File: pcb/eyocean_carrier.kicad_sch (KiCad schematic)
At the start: 9 parts, among them J1 SuperMini_L (TX..GPIO7), J2 SuperMini_R (5V..GPIO8), J3 CC1101_433MHz

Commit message: pcb: use 0603 for both decoupling capacitors
Move the 10 uF CC1101 decoupling cap from 0805 to the same 0603
hand-solder footprint as the 100 nF (use X5R, >= 6.3 V). Regenerated
schematic and board (3V3 rail and pad-1 positions unchanged), ERC/DRC
with schematic parity clean, JLCPCB Gerbers re-exported.
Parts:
- C2: footprint Capacitor_SMD:C_0805_2012Metric_Pad1.18x1.45mm_HandSolder -> Capacitor_SMD:C_0603_1608Metric_Pad1.08x0.95mm_HandSolder
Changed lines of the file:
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@@
 			)
 		)
-		(property "Footprint" "Capacitor_SMD:C_0805_2012Metric_Pad1.18x1.45mm_HandSolder"
+		(property "Footprint" "Capacitor_SMD:C_0603_1608Metric_Pad1.08x0.95mm_HandSolder"
 			(at 154.94 114.3 0)
 			(hide yes)

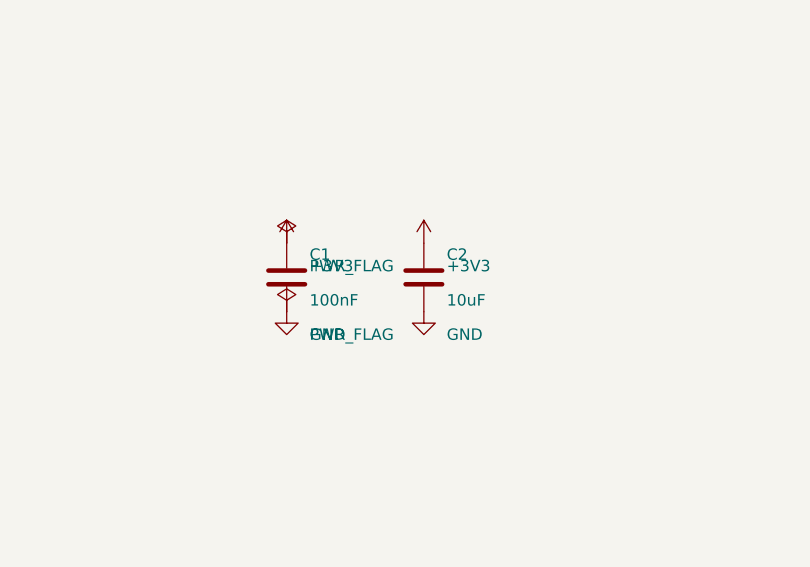
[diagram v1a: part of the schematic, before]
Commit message: pcb: single 10 uF decoupling capacitor
The CC1101 module already carries its own 100 nF next to the chip, so
the carrier only needs a local bulk cap for the TX current bursts. Drop
C2 and make C1 a 10 uF 0603 X5R 10 V (LCSC C19702, Samsung
CL10A106KP8NNNC); its GND stitching via now sits beside its pad.
Regenerated schematic and board, ERC/DRC with schematic parity clean,
JLCPCB Gerbers re-exported.
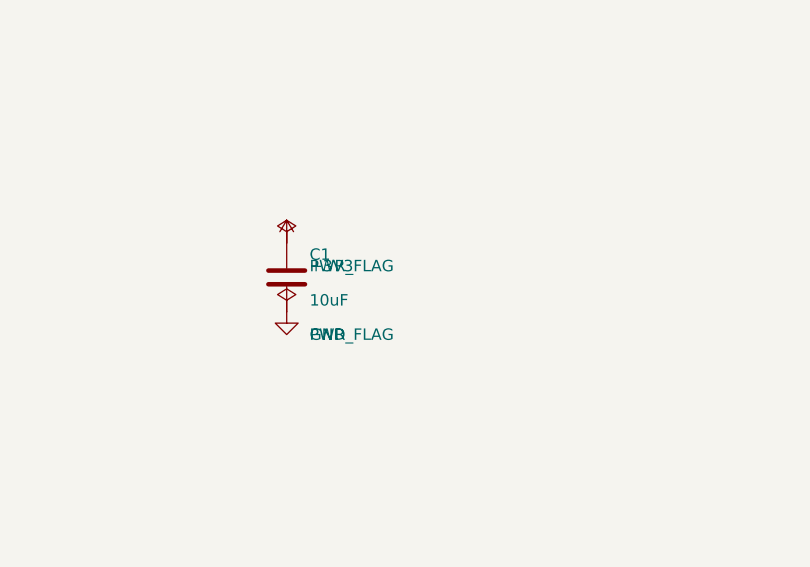
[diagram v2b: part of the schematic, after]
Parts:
- removed C2: 10uF, Capacitor_SMD:C_0603_1608Metric_Pad1.08x0.95mm_HandSolder, symbol Device:C
- C1: value 100nF -> 10uF
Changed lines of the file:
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@@
 			)
 		)
-		(property "Value" "100nF"
+		(property "Value" "10uF"
 			(at 142.24 116.84 0)
 			(show_name no)
@@
 			)
 		)
-		(property "Description" "CC1101 VDD decoupling"
+		(property "Description" "CC1101 VDD bulk decoupling, 10 uF X5R >= 10 V"
 			(at 139.7 114.3 0)
 			(hide yes)
@@
 					(unit 1)
 				)
-			)
-		)
-	)
-	(symbol
-		(lib_id "Device:C")
-		(at 154.94 114.3 0)
-		(unit 1)
-		(body_style 1)
-		(exclude_from_sim no)
-		(in_bom yes)
-		(on_board yes)
-		(in_pos_files yes)
-		(dnp no)
-		(property "Reference" "C2"
-			(at 157.48 111.76 0)
-			(show_name no)
-			(do_not_autoplace no)
-			(effects
-				(font
-					(size 1.27 1.27)
-				)
-				(justify left)
-			)
-		)
-		(property "Value" "10uF"
-			(at 157.48 116.84 0)
-			(show_name no)
-			(do_not_autoplace no)
-			(effects
-				(font
-					(size 1.27 1.27)
-				)
-				(justify left)
-			)
-		)
-		(property "Footprint" "Capacitor_SMD:C_0603_1608Metric_Pad1.08x0.95mm_HandSolder"
-			(at 154.94 114.3 0)
-			(hide yes)
-			(show_name no)
-			(do_not_autoplace no)
-			(effects
-				(font
-					(size 1.27 1.27)
-				)
-			)
-		)
-		(property "Datasheet" ""
-			(at 154.94 114.3 0)
-			(hide yes)
-			(show_name no)
-			(do_not_autoplace no)
-			(effects
-				(font
-					(size 1.27 1.27)
-				)
-			)
-		)
-		(property "Description" "CC1101 VDD decoupling"
-			(at 154.94 114.3 0)
-			(hide yes)
-			(show_name no)
-			(do_not_autoplace no)
-			(effects
-				(font
-					(size 1.27 1.27)
-				)
-			)
-		)
-		(pin "1"
-		)
-		(pin "2"
-		)
-		(instances
-			(project "eyocean_carrier"
-				(path "/a0c91d3c-5fdc-59af-b81d-66f690f70db9"
-					(reference "C2")
-					(unit 1)
-				)
-			)
-		)
-	)
-	(symbol
-		(lib_id "power:+3V3")
-		(at 154.94 110.49 0)
-		(unit 1)
-		(body_style 1)
-		(exclude_from_sim no)
-		(in_bom no)
-		(on_board no)
-		(in_pos_files no)
-		(dnp no)
-		(property "Reference" "#PWR07"
-			(at 157.48 107.95 0)
-			(hide yes)
-			(show_name no)
-			(do_not_autoplace no)
-			(effects
-				(font
-					(size 1.27 1.27)
-				)
-				(justify left)
-			)
-		)
-		(property "Value" "+3V3"
-			(at 157.48 113.03 0)
-			(show_name no)
-			(do_not_autoplace no)
-			(effects
-				(font
-					(size 1.27 1.27)
-				)
-				(justify left)
-			)
-		)
-		(property "Footprint" ""
-			(at 154.94 110.49 0)
-			(hide yes)
-			(show_name no)
-			(do_not_autoplace no)
-			(effects
-				(font
-					(size 1.27 1.27)
-				)
-			)
-		)
-		(property "Datasheet" ""
-			(at 154.94 110.49 0)
-			(hide yes)
-			(show_name no)
-			(do_not_autoplace no)
-			(effects
-				(font
-					(size 1.27 1.27)
-				)
-			)
-		)
-		(property "Description" ""
-			(at 154.94 110.49 0)
-			(hide yes)
-			(show_name no)
-			(do_not_autoplace no)
-			(effects
-				(font
-					(size 1.27 1.27)
-				)
-			)
-		)
-		(pin "1"
-		)
-		(instances
-			(project "eyocean_carrier"
-				(path "/a0c91d3c-5fdc-59af-b81d-66f690f70db9"
-					(reference "#PWR07")
-					(unit 1)
-				)
-			)
-		)
-	)
-	(symbol
-		(lib_id "power:GND")
-		(at 154.94 118.11 0)
-		(unit 1)
-		(body_style 1)
-		(exclude_from_sim no)
-		(in_bom no)
-		(on_board no)
-		(in_pos_files no)
-		(dnp no)
-		(property "Reference" "#PWR08"
-			(at 157.48 115.57 0)
-			(hide yes)
-			(show_name no)
-			(do_not_autoplace no)
-			(effects
-				(font
-					(size 1.27 1.27)
-				)
-				(justify left)
-			)
-		)
-		(property "Value" "GND"
-			(at 157.48 120.65 0)
-			(show_name no)
-			(do_not_autoplace no)
-			(effects
-				(font
-					(size 1.27 1.27)
-				)
-				(justify left)
-			)
-		)
-		(property "Footprint" ""
-			(at 154.94 118.11 0)
-			(hide yes)
-			(show_name no)
-			(do_not_autoplace no)
-			(effects
-				(font
-					(size 1.27 1.27)
-				)
-			)
-		)
-		(property "Datasheet" ""
-			(at 154.94 118.11 0)
-			(hide yes)
-			(show_name no)
-			(do_not_autoplace no)
-			(effects
-				(font
-					(size 1.27 1.27)
-				)
-			)
-		)
-		(property "Description" ""
-			(at 154.94 118.11 0)
-			(hide yes)
-			(show_name no)
-			(do_not_autoplace no)
-			(effects
-				(font
-					(size 1.27 1.27)
-				)
-			)
-		)
-		(pin "1"
-		)
-		(instances
-			(project "eyocean_carrier"
-				(path "/a0c91d3c-5fdc-59af-b81d-66f690f70db9"
-					(reference "#PWR08")
-					(unit 1)
-				)
